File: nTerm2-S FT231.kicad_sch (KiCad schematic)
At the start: 121 parts, among them J1 VGA, J2 Keyboard, J3 Mouse, J4 Line-out/Speaker, J5 RS-232 V.24, J6 USB_C_Receptacle_USB2.0_16P, J7 Line-out/Speaker, K1 IM41 3V, K2 IM41 3V, K3 IM41 3V, Q1 BC817, Q2 BC817, Q3 BC817, Q4 BC817, Q5 BC817, Q6 BC817, Q7 BC817, Q8 BC817, SW1 IO0, SW2 RESET, SW3 DEFAULTS, U1 ESP32-WROOM-32, U2 LM386, U3 MAX3232E, U4 DS2417, U5 NCP1117-3.3_SOT223, U6 USBLC6-2SC6, U7 FT231XS, Y1 32.768MHz

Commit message: Exported library and footprints to project local library for distribution.
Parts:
- C1, C25, C26, C27: footprint Capacitor_SMD:CP_Elec_6.3x7.7 -> Library:CP_Elec_6.3x7.7; symbol Device:C_Polarized -> Library:C_Polarized
- C10, C11, C12, C14, C17, C19, C21, C8, C9: footprint Capacitor_Tantalum_SMD:CP_EIA-3216-18_Kemet-A_Pad1.58x1.35mm_HandSolder -> Library:CP_EIA-3216-18_Kemet-A_Pad1.58x1.35mm_HandSolder; symbol Device:C_Polarized -> Library:C_Polarized
- C13, C18: footprint Capacitor_Tantalum_SMD:CP_EIA-6032-28_Kemet-C_Pad2.25x2.35mm_HandSolder -> Library:CP_EIA-6032-28_Kemet-C_Pad2.25x2.35mm_HandSolder; symbol Device:C_Polarized -> Library:C_Polarized
- C15, C16, C22, C24, C28, C29, C30, C31, C32, C33, C4, C5, C6, C7: footprint Capacitor_SMD:C_0603_1608Metric_Pad1.08x0.95mm_HandSolder -> Library:C_0603_1608Metric_Pad1.08x0.95mm_HandSolder; symbol Device:C -> Library:C
- C2: footprint Capacitor_SMD:CP_Elec_5x5.4 -> Library:CP_Elec_5x5.4; symbol Device:C_Polarized -> Library:C_Polarized
- C20: footprint Capacitor_Tantalum_SMD:CP_EIA-3528-21_Kemet-B_Pad1.50x2.35mm_HandSolder -> Library:CP_EIA-3528-21_Kemet-B_Pad1.50x2.35mm_HandSolder; symbol Device:C_Polarized -> Library:C_Polarized
- C23: footprint Capacitor_Tantalum_SMD:CP_EIA-7343-30_AVX-N_Pad2.25x2.55mm_HandSolder -> Library:CP_EIA-7343-30_AVX-N_Pad2.25x2.55mm_HandSolder; symbol Device:C_Polarized -> Library:C_Polarized
- C3: footprint Capacitor_SMD:C_0805_2012Metric_Pad1.18x1.45mm_HandSolder -> Library:C_0805_2012Metric_Pad1.18x1.45mm_HandSolder; symbol Device:C -> Library:C
- D10, D6, D8, D9: footprint Diode_SMD:D_SOD-123 -> Library:D_SOD-123; symbol Diode:BAT43W-V -> Library:BAT43W-V
- D11, D12: footprint Sporos_Tech_Footprints:DIALIGHT_LED_3MM_DOUBLE -> Library:DIALIGHT_LED_3MM_DOUBLE; symbol Device:LED_Dual_AKAK -> Library:LED_Dual_AKAK
- D3: footprint Diode_SMD:Nexperia_CFP3_SOD-123W -> Library:Nexperia_CFP3_SOD-123W; symbol Diode:1N5819 -> Library:1N5819
- D4: footprint Sporos_Tech_Footprints:DIALIGHT_LED_3MM_SINGLE -> Library:DIALIGHT_LED_3MM_SINGLE; symbol Sporos_Tech:LED pins reversed -> Library:LED pins reversed
- E1: footprint Sporos_Tech_Footprints:Gold Cap V-Type -> Library:Gold Cap V-Type; symbol Sporos_Tech:Gold Cap -> Library:Gold Cap
- H1, H2, H3, H4, H5, H6: footprint MountingHole:MountingHole_3.2mm_M3 -> Library:MountingHole_3.2mm_M3; symbol Mechanical:MountingHole -> Library:MountingHole
- J1: footprint Sporos_Tech_Footprints:DSUB-15-HD_Female_Horizontal_P2.29x1.98mm_EdgePinOffset8.35mm_Housed_MountingHolesOffset10.89mm -> Library:DSUB-15-HD_Female_Horizontal_P2.29x1.98mm_EdgePinOffset8.35mm_Housed_MountingHolesOffset10.89mm; symbol Connector:DE15_Receptacle_HighDensity_MountingHoles -> Library:DE15_Receptacle_HighDensity_MountingHoles
- J2, J3: footprint Custom_Footprints:Connector_Mini-DIN_Female_6Pin_2rows -> Library:Connector_Mini-DIN_Female_6Pin_2rows; symbol Sporos_Tech:Mini-DIN-6-alt -> Library:Mini-DIN-6-alt
- J4: footprint Sporos_Tech_Footprints:Jack_3.5mm_Ledino_KB3SPRS_Horizontal-alt -> Library:Jack_3.5mm_Ledino_KB3SPRS_Horizontal-alt; symbol Connector_Audio:AudioJack2_Ground_Switch -> Library:AudioJack2_Ground_Switch
- J5: footprint Sporos_Tech_Footprints:DSUB-9_Male_Horizontal_P2.77x2.84mm_EdgePinOffset4.94mm_Housed_MountingHolesOffset7.48mm -> Library:DSUB-9_Male_Horizontal_P2.77x2.84mm_EdgePinOffset4.94mm_Housed_MountingHolesOffset7.48mm; symbol Connector:DE9_Plug_MountingHoles -> Library:DE9_Plug_MountingHoles
- J6: footprint Sporos_Tech_Footprints:USB_C_Receptacle_Molex_213716-0001 -> Library:USB_C_Receptacle_Molex_213716-0001; symbol Connector:USB_C_Receptacle_USB2.0_16P -> Library:USB_C_Receptacle_USB2.0_16P
- J7: footprint Connector_PinHeader_2.54mm:PinHeader_1x02_P2.54mm_Vertical -> Library:PinHeader_1x02_P2.54mm_Vertical; symbol Connector_Generic:Conn_01x02 -> Library:Conn_01x02
- JP1: footprint Jumper:SolderJumper-3_P1.3mm_Open_RoundedPad1.0x1.5mm_NumberLabels -> Library:SolderJumper-3_P1.3mm_Open_RoundedPad1.0x1.5mm_NumberLabels; symbol Jumper:SolderJumper_3_Open -> Library:SolderJumper_3_Open
- K1, K2, K3: footprint Sporos_Tech_Footprints:Relay_DPDT_AXICOM_IMSeries_Gullwing -> Library:Relay_DPDT_AXICOM_IMSeries_Gullwing; symbol Relay:IM41 -> Library:IM41
- Q1, Q2, Q3, Q4, Q5, Q6, Q7, Q8: footprint Package_TO_SOT_SMD:SOT-23 -> Library:SOT-23; symbol Transistor_BJT:BC817 -> Library:BC817
- R1, R10, R11, R12, R13, R14, R15, R16, R17, R18, R19, R2, R20, R21, R22, R23, R24, R25, R26, R27, R28, R29, R3, R30, R31, R32, R33, R34, R35, R36, R37, R38, R39, R4, R40, R41, R42, R43, R5, R6, R7, R8, R9: footprint Resistor_SMD:R_0603_1608Metric_Pad0.98x0.95mm_HandSolder -> Library:R_0603_1608Metric_Pad0.98x0.95mm_HandSolder; symbol Device:R -> Library:R
- SW1, SW2, SW3: footprint Sporos_Tech_Footprints:SW_Tactile_SPST_Angled_PTS645Vx58-2LFS-alt -> Library:SW_Tactile_SPST_Angled_PTS645Vx58-2LFS-alt; symbol Switch:CK_KMS2xxGP -> Library:CK_KMS2xxGP
- U1: footprint RF_Module:ESP32-WROOM-32 -> Library:ESP32-WROOM-32; symbol RF_Module:ESP32-WROOM-32 -> Library:ESP32-WROOM-32
- U2: footprint Package_SO:SOIC-8_3.9x4.9mm_P1.27mm -> Library:SOIC-8_3.9x4.9mm_P1.27mm; symbol Amplifier_Audio:LM386 -> Library:LM386
- U3: footprint Package_SO:SOIC-16_3.9x9.9mm_P1.27mm -> Library:SOIC-16_3.9x9.9mm_P1.27mm; symbol Custom_Symbols_Library:MAX3232E -> Library:MAX3232E
- U4: footprint Package_SO_J-Lead:TSOC-6_3.76x3.94mm_P1.27mm -> Library:TSOC-6_3.76x3.94mm_P1.27mm; symbol Sporos_Tech:DS2417 -> Library:DS2417
- U5: footprint Package_TO_SOT_SMD:SOT-223-3_TabPin2 -> Library:SOT-223-3_TabPin2; symbol Regulator_Linear:NCP1117-3.3_SOT223 -> Library:NCP1117-3.3_SOT223
- U6: footprint Package_TO_SOT_SMD:SOT-23-6 -> Library:SOT-23-6; symbol Power_Protection:USBLC6-2SC6 -> Library:USBLC6-2SC6
- U7: footprint Package_SO:SSOP-20_3.9x8.7mm_P0.635mm -> Library:SSOP-20_3.9x8.7mm_P0.635mm; symbol Interface_USB:FT231XS -> Library:FT231XS
- Y1: footprint Crystal:Crystal_C38-LF_D3.0mm_L8.0mm_Horizontal -> Library:Crystal_C38-LF_D3.0mm_L8.0mm_Horizontal; symbol Device:Crystal -> Library:Crystal

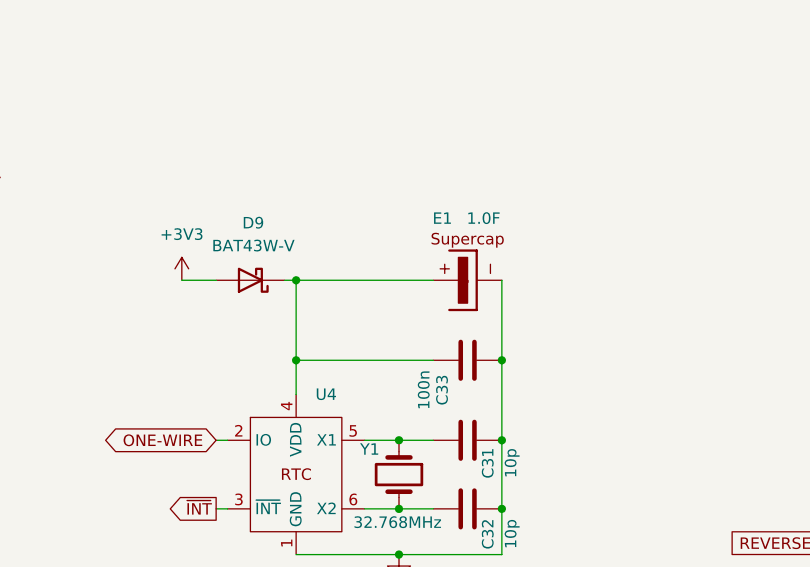
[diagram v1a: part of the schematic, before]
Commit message: Changed supercap to a CR2032 battery for timekeeping. Exported library. Fixed VGA footprint. Added a few more 3D footprints.
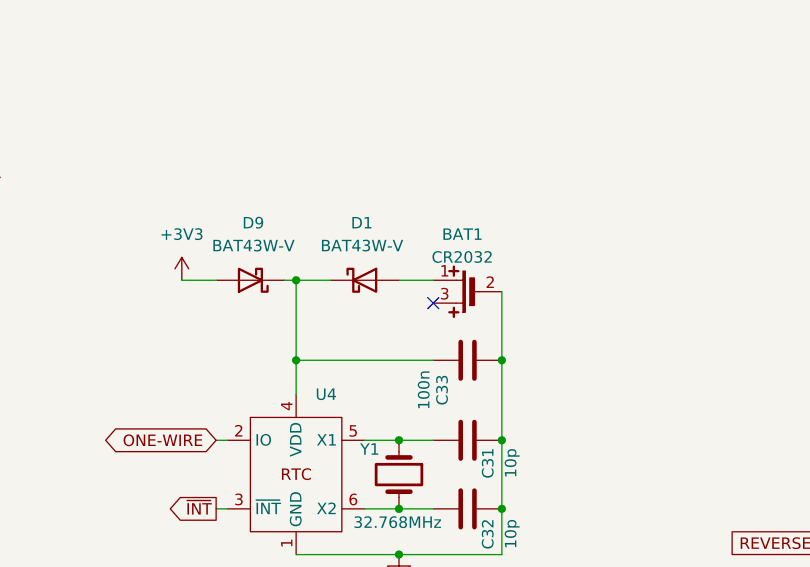
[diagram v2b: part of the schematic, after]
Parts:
- removed E1: 1.0F, Library:Gold Cap V-Type, symbol Library:Gold Cap
- added BAT1: CR2032, Sporos_Tech_Footprints:TE Connectivity CR2032 V, symbol nTerm2-S:CR2032_Battery_Holder
- added D1: BAT43W-V, Library:D_SOD-123, symbol nTerm2-S:BAT43W-V
- C1, C10, C11, C12, C13, C14, C17, C18, C19, C2, C20, C21, C23, C25, C26, C27, C8, C9: symbol Library:C_Polarized -> nTerm2-S:C_Polarized
- C15, C16, C22, C24, C28, C29, C3, C30, C31, C32, C33, C4, C5, C6, C7: symbol Library:C -> nTerm2-S:C
- D10, D6, D8, D9: symbol Library:BAT43W-V -> nTerm2-S:BAT43W-V
- D11, D12: symbol Library:LED_Dual_AKAK -> nTerm2-S:LED_Dual_AKAK
- D3: symbol Library:1N5819 -> nTerm2-S:1N5819
- D4: symbol Library:LED pins reversed -> nTerm2-S:LED pins reversed
- H1, H2, H3, H4, H5, H6: symbol Library:MountingHole -> nTerm2-S:MountingHole
- J1: footprint Library:DSUB-15-HD_Female_Horizontal_P2.29x1.98mm_EdgePinOffset8.35mm_Housed_MountingHolesOffset10.89mm -> Sporos_Tech_Footprints:DSUB-15-HD AssMann HD 15FW; symbol Library:DE15_Receptacle_HighDensity_MountingHoles -> nTerm2-S:DE15_Receptacle_HighDensity_MountingHoles
- J2, J3: symbol Library:Mini-DIN-6-alt -> nTerm2-S:Mini-DIN-6-alt
- J4: symbol Library:AudioJack2_Ground_Switch -> nTerm2-S:AudioJack2_Ground_Switch
- J5: footprint Library:DSUB-9_Male_Horizontal_P2.77x2.84mm_EdgePinOffset4.94mm_Housed_MountingHolesOffset7.48mm -> Connector_Dsub:DSUB-9_Pins_Horizontal_P2.77x2.84mm_EdgePinOffset7.70mm_Housed_MountingHolesOffset9.12mm; symbol Library:DE9_Plug_MountingHoles -> nTerm2-S:DE9_Plug_MountingHoles
- J6: symbol Library:USB_C_Receptacle_USB2.0_16P -> nTerm2-S:USB_C_Receptacle_USB2.0_16P
- J7: symbol Library:Conn_01x02 -> nTerm2-S:Conn_01x02
- JP1: symbol Library:SolderJumper_3_Open -> nTerm2-S:SolderJumper_3_Open
- K1, K2, K3: symbol Library:IM41 -> nTerm2-S:IM41
- Q1, Q2, Q3, Q4, Q5, Q6, Q7, Q8: symbol Library:BC817 -> nTerm2-S:BC817
- R1, R10, R11, R12, R13, R14, R15, R16, R17, R18, R19, R2, R20, R21, R22, R23, R24, R25, R26, R27, R28, R29, R3, R30, R31, R32, R33, R34, R35, R36, R37, R38, R39, R4, R40, R41, R42, R43, R5, R6, R7, R8, R9: symbol Library:R -> nTerm2-S:R
- SW1, SW2, SW3: symbol Library:CK_KMS2xxGP -> nTerm2-S:CK_KMS2xxGP
- U1: symbol Library:ESP32-WROOM-32 -> nTerm2-S:ESP32-WROOM-32
- U2: symbol Library:LM386 -> nTerm2-S:LM386
- U3: symbol Library:MAX3232E -> nTerm2-S:MAX3232E
- U4: symbol Library:DS2417 -> nTerm2-S:DS2417
- U5: symbol Library:NCP1117-3.3_SOT223 -> nTerm2-S:NCP1117-3.3_SOT223
- U6: symbol Library:USBLC6-2SC6 -> nTerm2-S:USBLC6-2SC6
- U7: symbol Library:FT231XS -> nTerm2-S:FT231XS
- Y1: symbol Library:Crystal -> nTerm2-S:Crystal
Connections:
- net GND: now also BAT1.2
- net at C33.1, D9.1 (K), U4.4 (VDD): now also D1.1 (K)
- new net: BAT1.1, D1.2 (A)
- no-connect marks 25 -> 26
